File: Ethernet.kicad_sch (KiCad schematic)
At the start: 0 parts

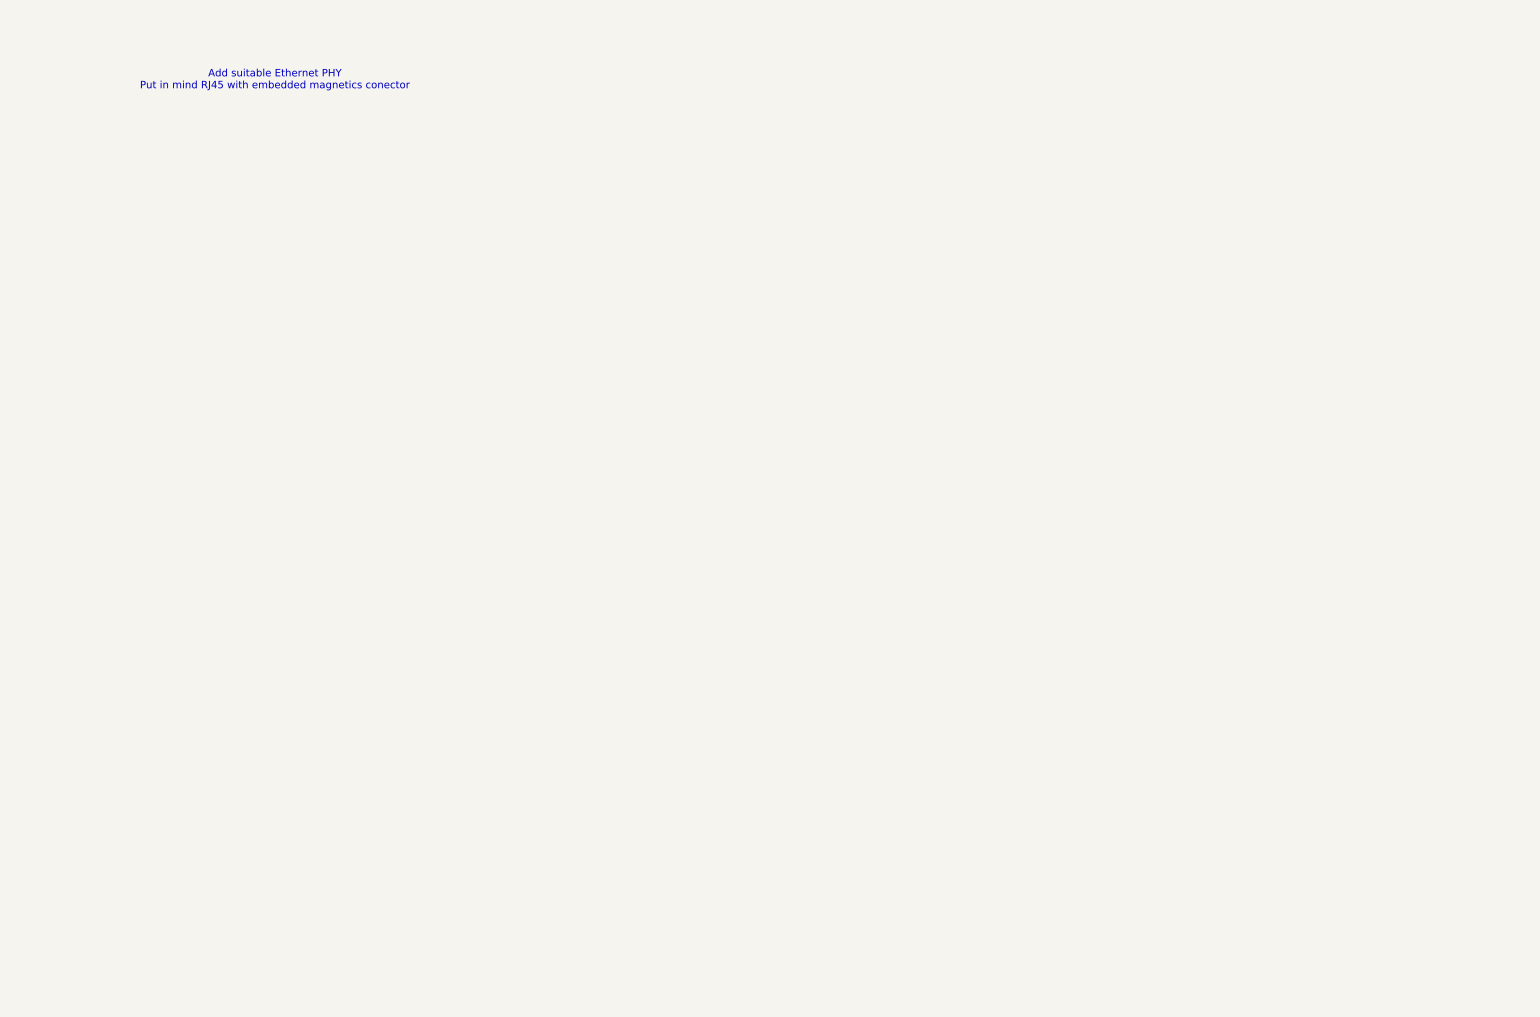
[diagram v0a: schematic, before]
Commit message: added Ethernet and SPI interface
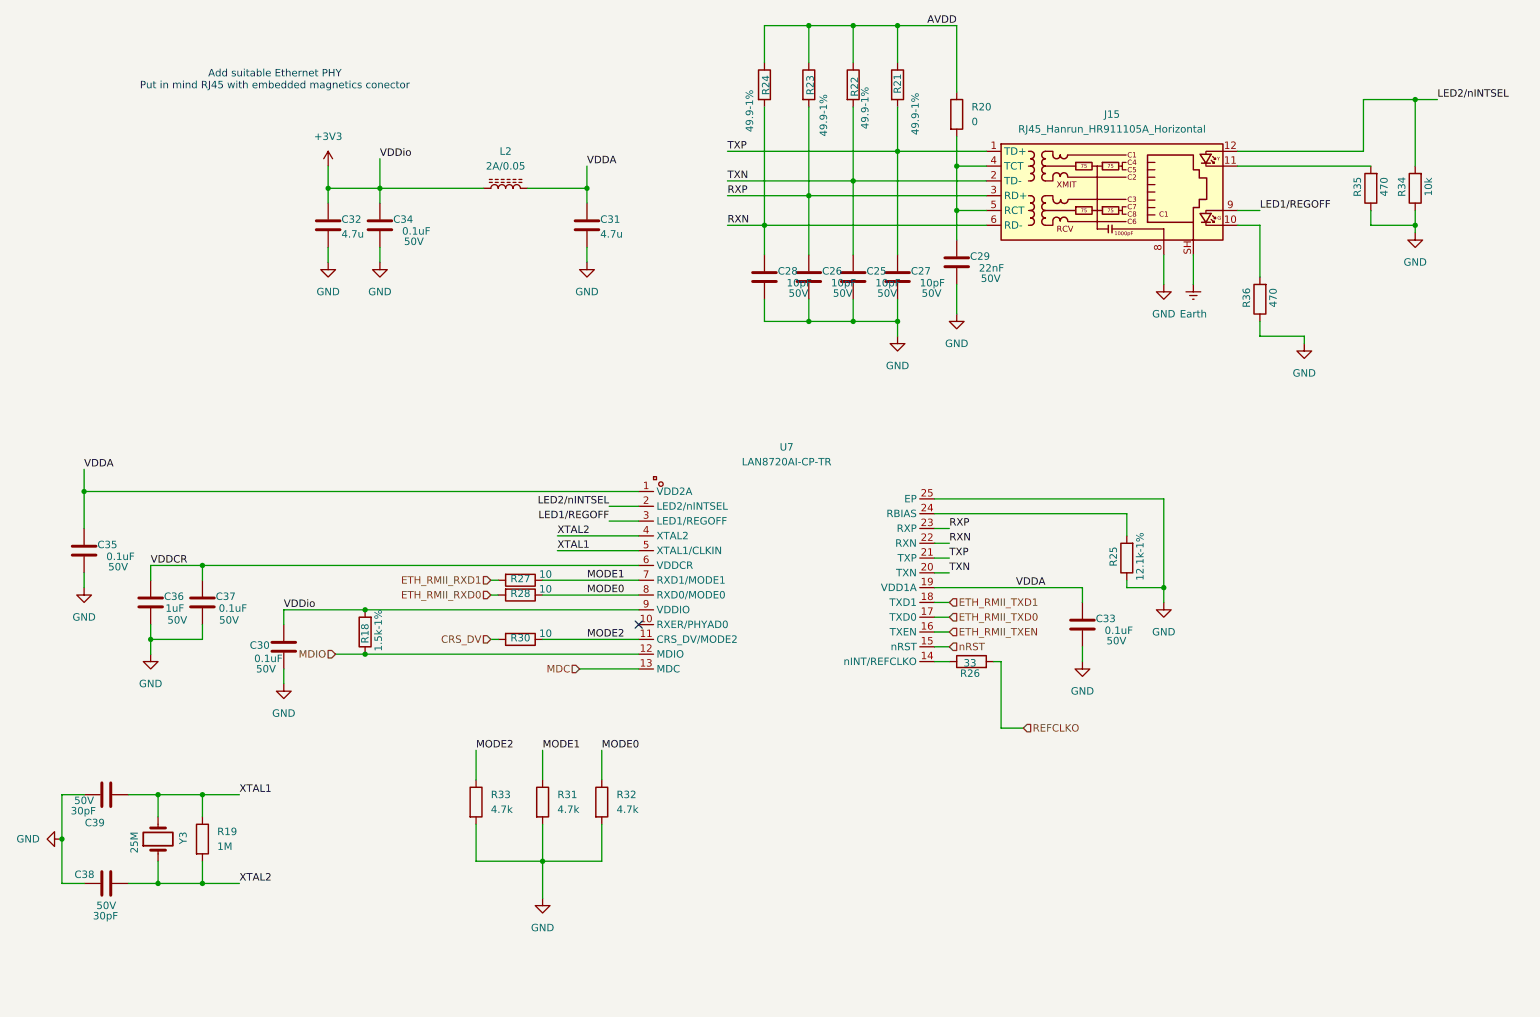
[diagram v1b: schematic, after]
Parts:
- added C25, C26, C27, C28: 10pF, symbol Device:C
- added C29: 22nF, symbol Device:C
- added C30, C33, C34, C35, C37: 0.1uF, symbol Device:C
- added C31, C32: 4.7u, symbol Device:C
- added C36: 1uF, symbol Device:C
- added C38, C39: 30pF, symbol Device:C
- added J15: RJ45_Hanrun_HR911105A_Horizontal, Connector_RJ:RJ45_Hanrun_HR911105A_Horizontal, symbol Connector:RJ45_Hanrun_HR911105A_Horizontal
- added L2: 2A/0.05, symbol Device:L_Ferrite
- added R18: 1.5k-1%, symbol Device:R
- added R19: 1M, symbol Device:R
- added R20: 0, symbol Device:R
- added R21, R22, R23, R24: 49.9-1%, symbol Device:R
- added R25: 12.1k-1%, symbol Device:R
- added R26: 33, symbol Device:R
- added R27, R28, R30: 10, symbol Device:R
- added R31, R32, R33: 4.7k, symbol Device:R
- added R34: 10k, symbol Device:R
- added R35, R36: 470, symbol Device:R
- added U7: LAN8720AI-CP-TR, EasyEDA:QFN-24_L4.0-W4.0-P0.50-BL-EP2.6, symbol EasyEDA:LAN8720AI-CP-TR
- added Y3: 25M, symbol Device:Crystal
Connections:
- new net: R25.2, U7.24 (RBIAS)
- new net: J15.11, R35.2
- new net: J15.10, R36.2
- new net: R26.1, U7.14 (nINT/REFCLKO)
- new net: C29.1, J15.4 (TCT), J15.5 (RCT), R20.2
- new net +3V3: C30.1, C32.1, C34.1, L2.1, R18.2, U7.9 (VDDIO)
- new net AVDD: R20.1, R21.1, R22.1, R23.1, R24.1
- new net CRS_DV: R30.2
- new net ETH_RMII_RXD0: R28.2
- new net ETH_RMII_RXD1: R27.2
- new net ETH_RMII_TXD0: U7.17 (TXD0)
- new net ETH_RMII_TXD1: U7.18 (TXD1)
- new net ETH_RMII_TXEN: U7.16 (TXEN)
- new net Earth: J15.SH
- new net GND: C25.2, C26.2, C27.2, C28.2, C29.2, C30.2, C31.2, C32.2, C33.2, C34.2, C35.2, C36.2, C37.2, C38.1, C39.1, J15.8, R25.1, R31.2, R32.2, R33.2, R34.1, R35.1, R36.1, U7.25 (EP)
- new net LED1/REGOFF: J15.9, U7.3 (LED1/REGOFF)
- new net LED2/nINTSEL: J15.12, R34.2, U7.2 (LED2/nINTSEL)
- new net MDC: U7.13 (MDC)
- new net MDIO: R18.1, U7.12 (MDIO)
- new net MODE0: R28.1, R32.1, U7.8 (RXD0/MODE0)
- new net MODE1: R27.1, R31.1, U7.7 (RXD1/MODE1)
- new net MODE2: R30.1, R33.1, U7.11 (CRS_DV/MODE2)
- new net REFCLKO: R26.2
- new net RXN: C28.1, J15.6 (RD-), R24.2, U7.22 (RXN)
- new net RXP: C26.1, J15.3 (RD+), R23.2, U7.23 (RXP)
- new net TXN: C25.1, J15.2 (TD-), R22.2, U7.20 (TXN)
- new net TXP: C27.1, J15.1 (TD+), R21.2, U7.21 (TXP)
- new net VDDA: C31.1, C33.1, C35.1, L2.2, U7.1 (VDD2A), U7.19 (VDD1A)
- new net VDDCR: C36.1, C37.1, U7.6 (VDDCR)
- new net XTAL1: C39.2, R19.1, U7.5 (XTAL1/CLKIN), Y3.2
- new net XTAL2: C38.2, R19.2, U7.4 (XTAL2), Y3.1
- new net nRST: U7.15 (nRST)
- no-connect marks 0 -> 1

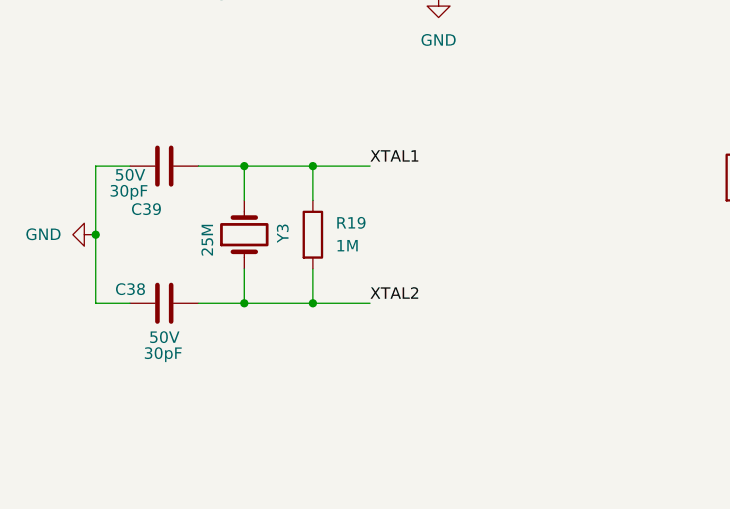
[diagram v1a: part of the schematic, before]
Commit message: Schematic--Footprint link
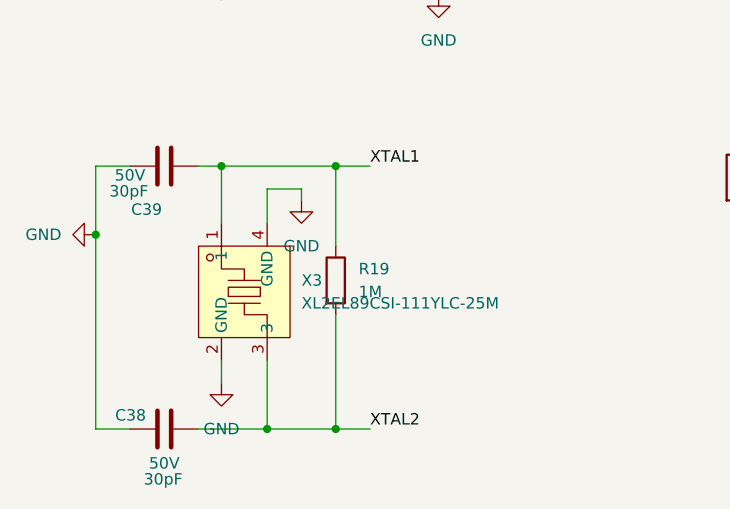
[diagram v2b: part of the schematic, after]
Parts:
- removed Y3: 25M, symbol Device:Crystal
- added X3: XL2EL89CSI-111YLC-25M, EasyEDA:CRYSTAL-SMD_4P-L3.2-W2.5-BL, symbol EasyEDA:XL2EL89CSI-111YLC-25M
- C25, C26, C27, C28, C29, C30, C31, C32, C33, C34, C35, C36, C37, C38, C39: footprint (none) -> Capacitor_SMD:C_0805_2012Metric
- L2: footprint (none) -> Inductor_SMD:L_1206_3216Metric
- R18, R19, R20, R21, R22, R23, R24, R25, R26, R27, R28, R30, R31, R32, R33, R34, R35, R36: footprint (none) -> Resistor_SMD:R_0805_2012Metric
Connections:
- net GND: now also X3.2 (GND), X3.4 (GND)
- net XTAL1: now also X3.1
- net XTAL2: now also X3.3
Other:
- moved on the sheet: C38, R19
